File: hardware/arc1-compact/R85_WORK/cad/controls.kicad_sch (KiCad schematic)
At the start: 20 parts, among them J10 F133 UART0, SW10 Y, SW11 L, SW12 R, SW13 START, SW14 SELECT, SW15 HOME, SW3 UP, SW4 DOWN, SW5 LEFT, SW6 RIGHT, SW7 A, SW8 B, SW9 X

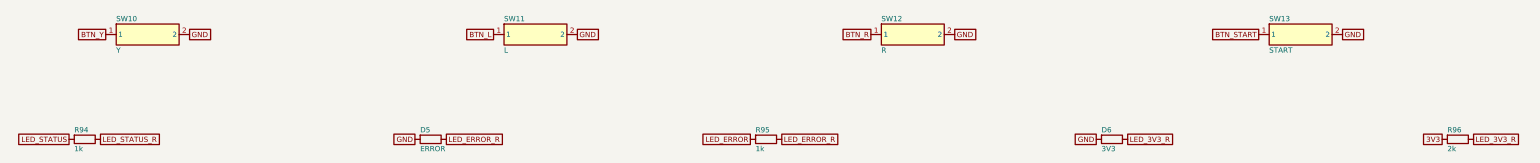
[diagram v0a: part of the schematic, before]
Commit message: ARC-1 Compact R8.5: ECP5 board sheet (power tree, sysCONFIG SSPI, JTAG), regenerated KiCad (ERC 0), R8.5 rule checker, pin matrices + generated LPF, routed reproducible bitstream
Co-Authored-By: Claude Opus 5.5 <noreply@anthropic.com>
Claude-Session: https://claude.ai/code/session_01UkiuLdbjDvK75uDzAPKsGs
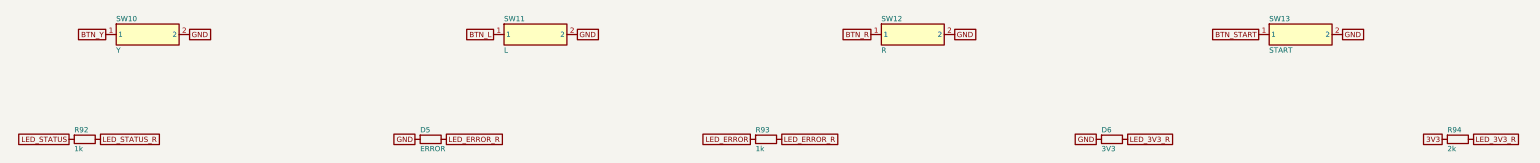
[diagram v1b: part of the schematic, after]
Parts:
- removed R95: 1k, Resistor_SMD:R_0402_1005Metric, symbol ARC1_R08:R0402
- removed R96: 2k, Resistor_SMD:R_0402_1005Metric, symbol ARC1_R08:R0402
- added R92, R93: 1k, Resistor_SMD:R_0402_1005Metric, symbol ARC1_R85:R0402
- D4, D5, D6: symbol ARC1_R08:LED -> ARC1_R85:LED
- J10: symbol ARC1_R08:HDR_1x3 -> ARC1_R85:HDR_1x3
- R94: value 1k -> 2k; symbol ARC1_R08:R0402 -> ARC1_R85:R0402; LCSC (none) -> C4109; MPN (none) -> 0402WGF2001TCE; Manufacturer (none) -> UNI-ROYAL; Reuse (none) -> SLIM4_R26_BOM_LINE (re-validate)
- SW10, SW11, SW12, SW13, SW14, SW15, SW3, SW4, SW5, SW6, SW7, SW8, SW9: symbol ARC1_R08:SW_B3U -> ARC1_R85:SW_B3U
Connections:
- net 3V3: now also R94.1
- net LED_3V3_R: now also R94.2
- net LED_ERROR: now also R93.1
- net LED_ERROR_R: now also R93.2
- net LED_STATUS: now also R92.1; no longer R94.1
- net LED_STATUS_R: now also R92.2; no longer R94.2
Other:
- title: ARC-1 Compact R08: Game buttons, LEDs, debug UART -> ARC-1 Compact R8.5: Game buttons, LEDs, debug UART
- moved on the sheet: R94
